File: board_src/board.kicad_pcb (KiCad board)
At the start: 2 copper layers, 113 parts, among them IC1 PCF8563TS_4,118, IC2 M24C02-WMN6TP, IC3 DS18B20+, IC5 MCP3202-CI_MS, J1 Conn_01x05, J10 Conn_01x01_Pin, J11 Conn_01x03, J12 112J-TDAR-R01, J13 Conn_01x03, J14 Conn_01x07, J15 Conn_01x03, J16 Conn_01x05, J17 Conn_01x05, J18 Conn_02x20_Counter_Clockwise, J19 Conn_02x07_Odd_Even, J2 Conn_01x05, J20 Conn_02x20_Counter_Clockwise, J21 Conn_02x20_Counter_Clockwise, J22 Conn_02x20_Counter_Clockwise, J23 Conn_01x04, J24 Conn_01x08, J25 Conn_01x04, J27 USB4135-GF-A, J29 Conn_01x08, J3 Conn_01x06, J30 Conn_01x05, J31 Conn_01x05, J4 Conn_01x04, J5 Conn_01x08, J6 Conn_01x03, J8 Conn_01x03, J9 Conn_01x02_Pin, Q1 NPN, Q2 SS8550, Q3 SS8550, Q4 SS8550, Q5 SS8550, Q6 BC107, U1 Pico, U4 Pico, Y2 Crystal

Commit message: wersja z FT232RN
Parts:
- removed BT1: 3012, footprints:3012
- removed C3, C7: 10uF, Capacitor_SMD:C_0201_0603Metric
- removed C5, C6: 100uF, Capacitor_SMD:C_0201_0603Metric
- removed D12, D13: 1N4148WT, Diode_SMD:D_SOD-523
- removed Q6: BC107, OptoDevice:Osram_SFH3710
- removed R17, R18: 4.7k, Resistor_SMD:R_0201_0603Metric
- added D1: D_Schottky, Diode_SMD:D_1206_3216Metric, F.Cu at (116.5, 18.3)
- added IC4: FT232RNL-TUBE, footprints:SOP65P780X200-28N, F.Cu at (29.9, 74.5)
- added J32: Conn_02x05_Odd_Even, Connector_PinHeader_2.54mm:PinHeader_2x05_P2.54mm_Vertical, F.Cu at (41.7, 71.8)
- added J7: Conn_01x16_Socket, Connector_PinSocket_2.54mm:PinSocket_1x16_P2.54mm_Vertical, F.Cu at (129.8, 124.3)
- added LED10: red, footprints:LEDC1608X80N, F.Cu at (37.3, 65.5)
- added LED11: green, footprints:LEDC1608X100N, F.Cu at (40.3, 65.6)
- added Q7: BC107, OptoDevice:Osram_SFH3710, F.Cu at (163.6, 162.2)
- added R4: R, Resistor_SMD:R_1206_3216Metric, F.Cu at (163.7, 164.2)
- added R43: 4.7k, Resistor_SMD:R_1206_3216Metric, F.Cu at (49.4, 32.9)
- added R44: 4.7k, Resistor_SMD:R_1206_3216Metric, F.Cu at (49.4, 35.2)
- added R5: 1k, Resistor_SMD:R_1206_3216Metric, F.Cu at (45.0, 64.2)
- added SW1: SW_MEC_5E, Button_Switch_THT:SW_PUSH_6mm_H9.5mm, F.Cu at (93.9, 158.7)
- C1: footprint Capacitor_SMD:C_0201_0603Metric -> Capacitor_SMD:C_1206_3216Metric
- C2: value C -> C_Small; footprint Capacitor_SMD:C_0201_0603Metric -> Capacitor_SMD:C_1206_3216Metric
- C4: footprint Capacitor_SMD:C_1808_4520Metric -> Capacitor_SMD:C_1206_3216Metric_Pad1.33x1.80mm_HandSolder
- J10: value Conn_01x01_Pin -> Conn_01x02_Pin; footprint Connector_PinHeader_2.54mm:PinHeader_1x01_P2.54mm_Vertical -> Connector_PinHeader_2.54mm:PinHeader_1x02_P2.54mm_Vertical
- J6: value Conn_01x03 -> Conn_01x02_Pin; footprint Connector_PinHeader_2.54mm:PinHeader_1x03_P2.54mm_Vertical -> Connector_PinHeader_2.54mm:PinHeader_1x02_P2.54mm_Vertical
- J8: value Conn_01x03 -> Conn_01x01_Pin; footprint Connector_PinHeader_2.54mm:PinHeader_1x03_P2.54mm_Vertical -> Connector_PinHeader_2.54mm:PinHeader_1x01_P2.54mm_Vertical
- R1, R11, R12, R14, R15, R16, R2, R20, R21, R22, R23, R35, R36, R37, R38, R39, R40, R41, R42: footprint Resistor_SMD:R_0201_0603Metric -> Resistor_SMD:R_1206_3216Metric
- R19: value 103 -> 10k; footprint Resistor_SMD:R_0201_0603Metric -> Resistor_SMD:R_1206_3216Metric
- R3: value R -> 1k; footprint Resistor_SMD:R_0201_0603Metric -> Resistor_SMD:R_1206_3216Metric
- R31, R32, R33, R34: value 103 -> 10k
- moved R3 221.9 mm to (45.0, 66.9), turned to 180 degrees
- moved PS1 166.7 mm to (21.1, 63.2)
- moved J8 146.4 mm to (16.3, 29.8), turned to 0 degrees
- moved S3 114.4 mm to (114.4, 78.9), turned to 90 degrees
- moved RV1 111.4 mm to (157.5, 164.5)
- moved S4 100.9 mm to (106.4, 78.9), turned to 90 degrees
- moved S1 97.1 mm to (46.6, 19.6), turned to 0 degrees
- moved DS4 93.3 mm to (129.8, 124.3)
- moved S2 91.8 mm to (61.5, 19.6), turned to 0 degrees
- moved J6 90.2 mm to (24.8, 36.6), turned to 180 degrees
- moved R2 88.8 mm to (21.3, 85.3), turned to 0 degrees
- moved S5 88.2 mm to (98.3, 78.9), turned to 90 degrees
- moved R14 88.0 mm to (21.3, 87.6), turned to 0 degrees
- moved J13 86.8 mm to (22.7, 99.1), turned to 180 degrees
- moved Q1 83.6 mm to (21.8, 107.8)
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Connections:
- net /b1 renamed VBUS
- net /b2 renamed VSYS
- net Net-(IC1-CLKOUT) renamed /Zegar czasu rzeczywistego RTC/CLKOUT
- net Net-(IC1-~{INT}) renamed /Zegar czasu rzeczywistego RTC/INT
- C2 pad 1: GND -> Net-(IC4-3V3OUT)
- C2 pad 2: Net-(D12-K) -> GND
- C4 pad 2: Net-(J4-Pin_1) -> GND
- DS4 pad 1: GND -> unconnected-(DS4-VSS-Pad1)
- DS4 pad 10: /Wyświetlacz LCD/D3 -> unconnected-(DS4-DB3-Pad10)
- DS4 pad 11: /Wyświetlacz LCD/D4 -> unconnected-(DS4-DB4-Pad11)
- DS4 pad 12: /Wyświetlacz LCD/D5 -> unconnected-(DS4-DB5-Pad12)
- DS4 pad 13: /Wyświetlacz LCD/D6 -> unconnected-(DS4-DB6-Pad13)
- DS4 pad 14: /Wyświetlacz LCD/D7 -> unconnected-(DS4-DB7-Pad14)
- DS4 pad 15: Net-(DS4-A_1) -> unconnected-(DS4-A_1-Pad15)
- DS4 pad 16: +3.3V -> unconnected-(DS4-K_1-Pad16)
- DS4 pad 2: +3.3V -> unconnected-(DS4-VDD-Pad2)
- DS4 pad 3: Net-(DS4-VO) -> unconnected-(DS4-VO-Pad3)
- DS4 pad 4: /Wyświetlacz LCD/RS -> unconnected-(DS4-RS-Pad4)
- DS4 pad 5: /Wyświetlacz LCD/R/W -> unconnected-(DS4-R/~{W}-Pad5)
- DS4 pad 6: /Wyświetlacz LCD/E -> unconnected-(DS4-E-Pad6)
- DS4 pad 7: /Wyświetlacz LCD/D0 -> unconnected-(DS4-DB0-Pad7)
- DS4 pad 8: /Wyświetlacz LCD/D1 -> unconnected-(DS4-DB1-Pad8)
- DS4 pad 9: /Wyświetlacz LCD/D2 -> unconnected-(DS4-DB2-Pad9)
- IC2 pad 7: Net-(IC2-~{WC}) -> GND
- J10 pad 1: Net-(IC2-~{WC}) -> Net-(IC1-SDA)
- J12 pad 6: GND -> +3.3V
- J27 pad A9: +3.3V -> Net-(D1-A)
- J27 pad B9: +3.3V -> +5V
- J4 pad 1: Net-(J4-Pin_1) -> Net-(IC5-VDD/VREF)
- J6 pad 1: Net-(J6-Pin_1) -> Net-(IC2-SDA)
- J6 pad 2: Net-(J6-Pin_2) -> Net-(IC2-SCL)
- J8 pad 1: Net-(J8-Pin_1) -> GND
- PS1 pad 5: +3.3V -> GND
- R3 pad 1: Net-(Q6-B) -> +5V
- R3 pad 2: /Wyświetlacz LCD/BL -> Net-(LED11-A)
- RV1 pad 2: Net-(DS4-VO) -> Net-(J7-Pin_3)
- U1 pad 41: Net-(J8-Pin_3) -> unconnected-(U1-SWCLK-Pad41)_1
- U1 pad 42: Net-(J8-Pin_2) -> unconnected-(U1-GND-Pad42)_1
- U1 pad 43: Net-(J8-Pin_1) -> unconnected-(U1-SWDIO-Pad43)_1
- U4 pad 41: Net-(J6-Pin_3) -> unconnected-(U4-SWCLK-Pad41)_1
- U4 pad 42: Net-(J6-Pin_2) -> unconnected-(U4-GND-Pad42)
- U4 pad 43: Net-(J6-Pin_1) -> unconnected-(U4-SWDIO-Pad43)_1
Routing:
- net Net-(J13-Pin_3): track 0.00 -> 13.5 mm
- net Net-(J13-Pin_2): track 0.00 -> 13.1 mm
- net Net-(VR2-WIPER): track 0.00 -> 13.0 mm
- net Net-(VR1-WIPER): track 0.00 -> 7.04 mm
- net Net-(J13-Pin_1): track 0.00 -> 6.30 mm
- net Net-(J8-Pin_3): track 5.31 -> 0.00 mm
- net Net-(J8-Pin_2): track 5.31 -> 0.00 mm
- net Net-(J8-Pin_1): track 5.31 -> 0.00 mm
- net Net-(J6-Pin_3): track 5.08 -> 0.00 mm
- net Net-(J6-Pin_2): track 5.08 -> 0.00 mm
- net Net-(J6-Pin_1): track 5.08 -> 0.00 mm
- net Net-(LS1-+): track 0.00 -> 4.89 mm
- net Net-(LED4-A): track 5.49 -> 1.23 mm
- net Net-(LED7-A): track 4.85 -> 0.89 mm
- net Net-(LED9-A): track 5.60 -> 1.65 mm
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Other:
- board text added: "BL"
- board text added: "BUZ"
- board text added: "C0"
- board text added: "C1"
- board text added: "CS"
- board text added: "D0"
- board text added: "D1"
- board text added: "D2"
- board text added: "D3"
- board text added: "D4"
- board text added: "D5"
- board text added: "D6"
- board text added: "D7"
- board text added: "DCD"
- board text added: "DSR"
- board text added: "DTR"
- board text added: "E"
- board text added: "E0"
- board text added: "MCP3202"
- board text added: "POT1"
- board text added: "POT2"
- board text added: "RI"
- board text added: "RS"
- board text added: "RTS"
- board text added: "RW"
- board text added: "RXD"
- board text added: "SCL"
- board text added: "SDA"
- board text added: "TXD"
- board text added: "VCC"
- board text removed: "WC"

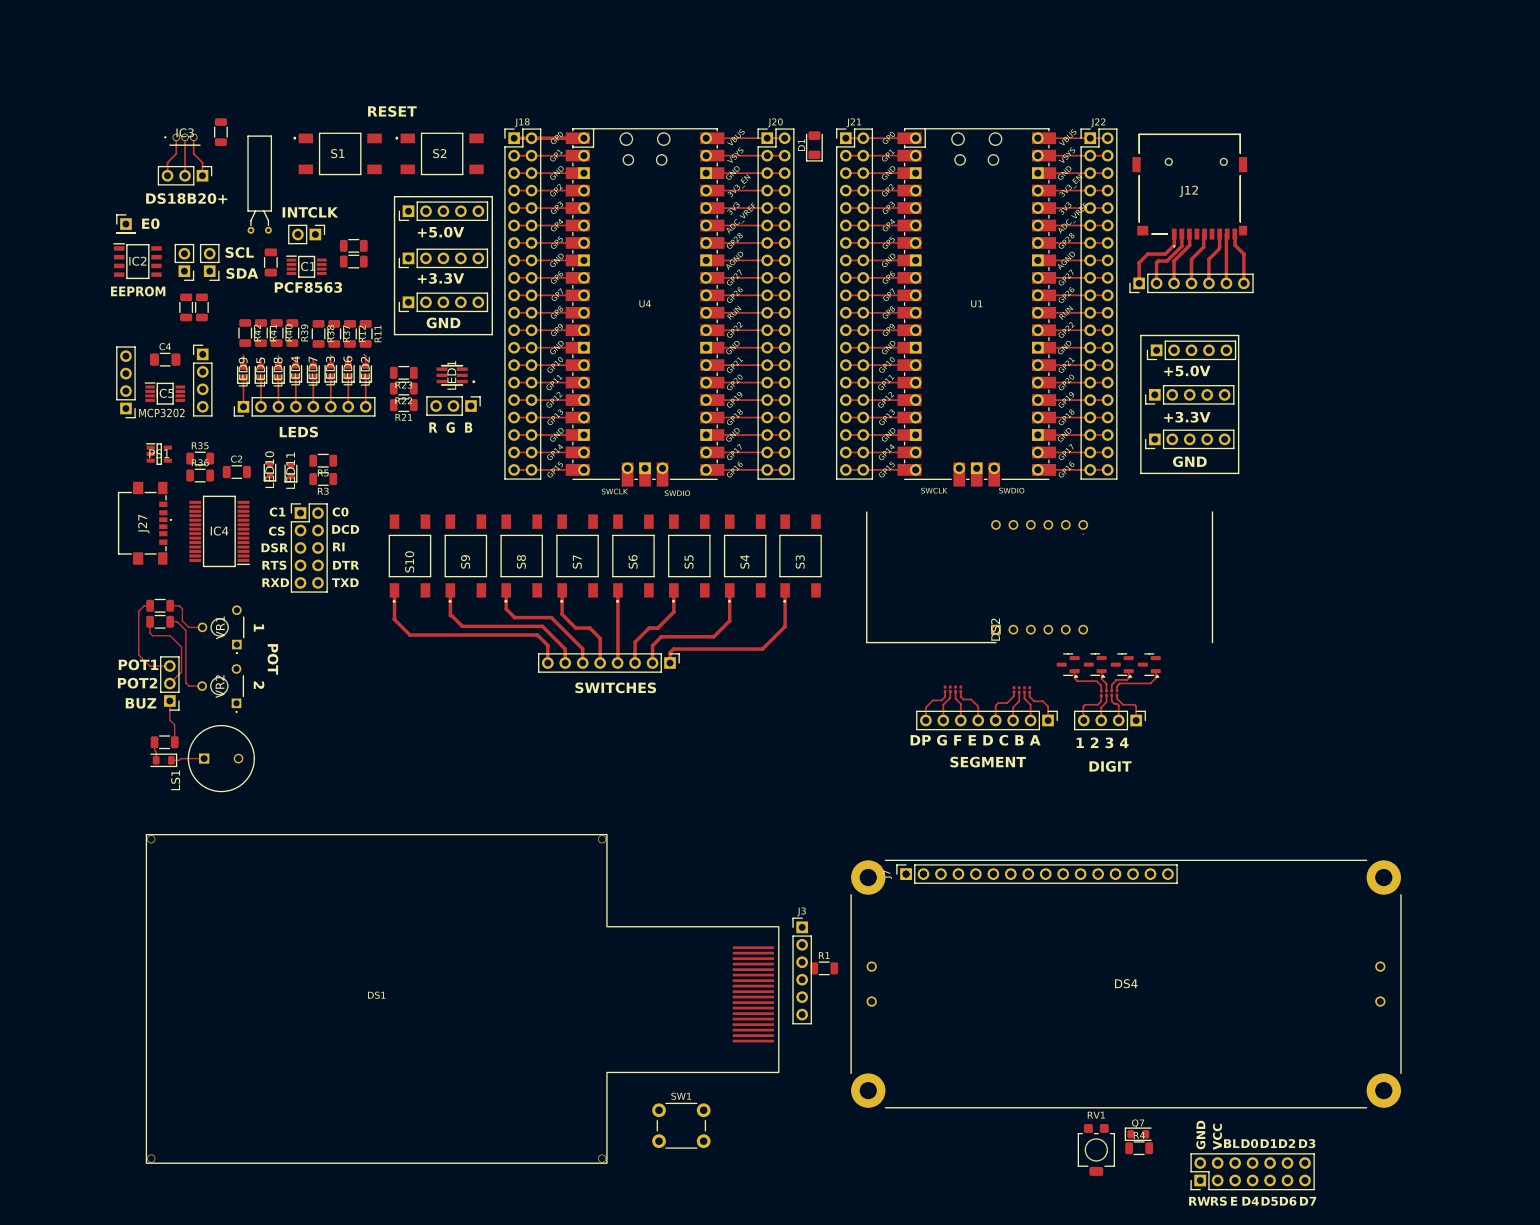
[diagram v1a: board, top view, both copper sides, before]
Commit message: Wersja ze sciezkami miedzianymi
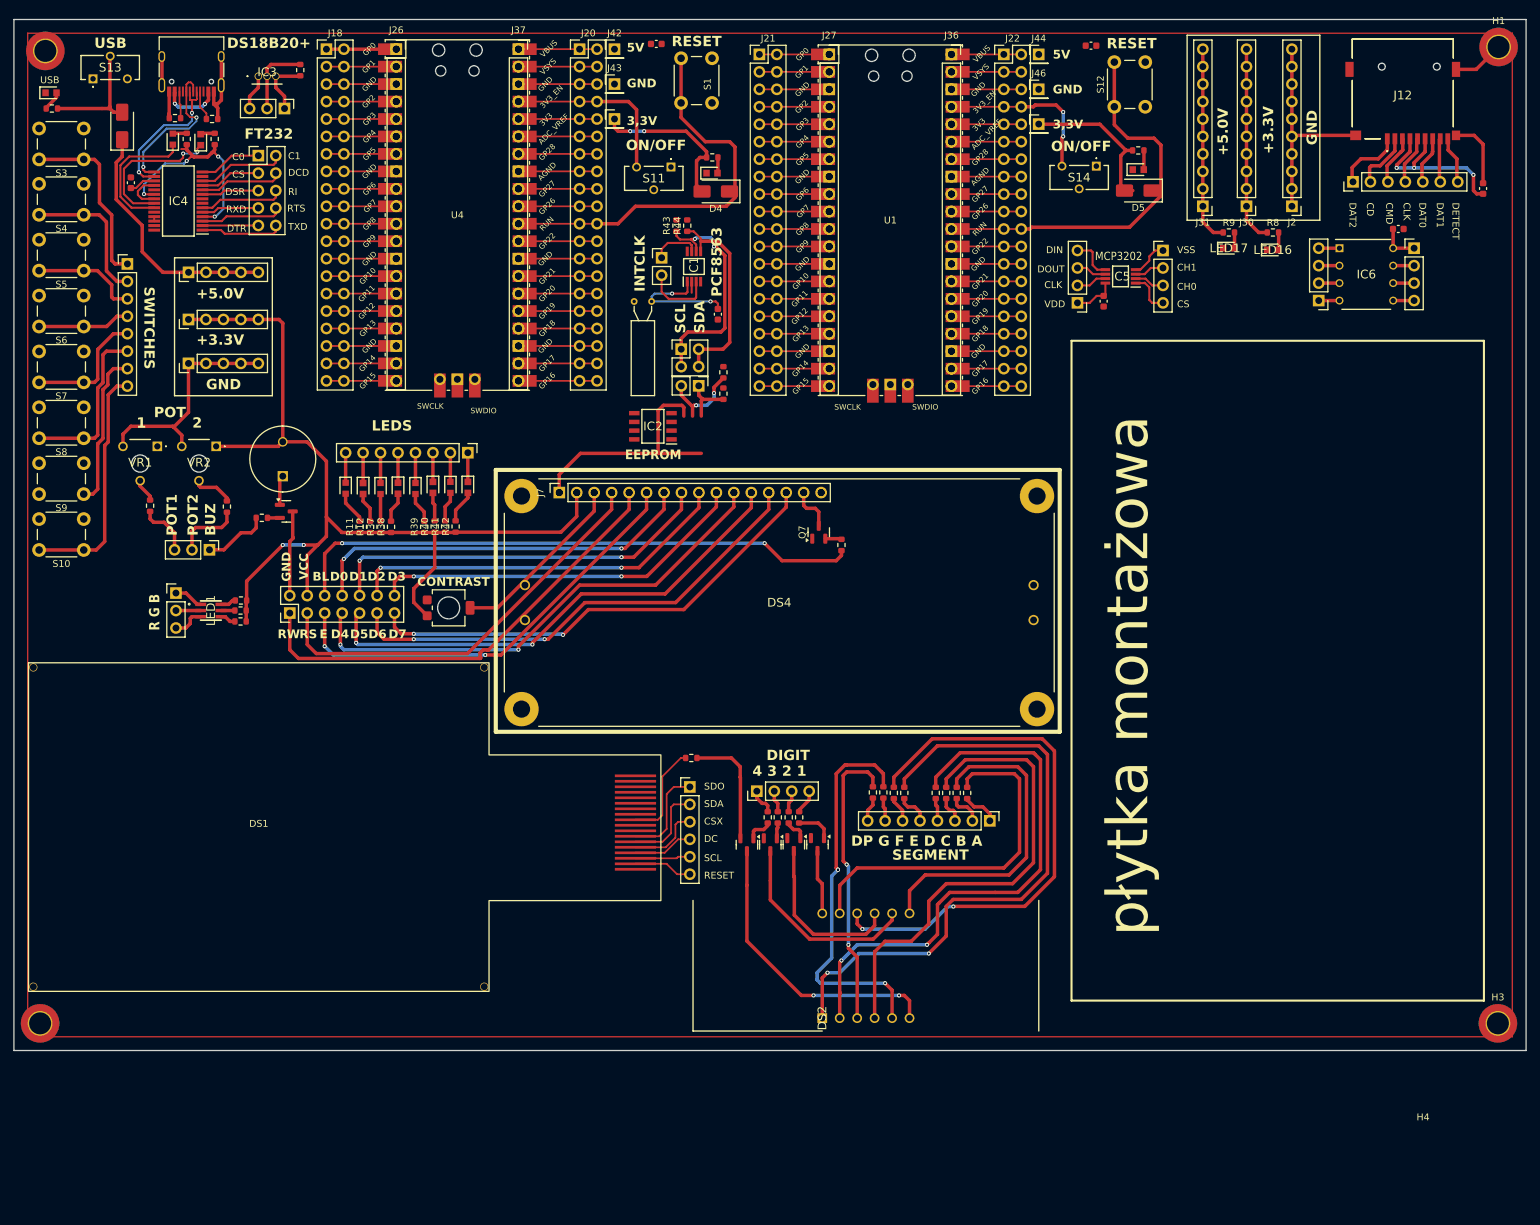
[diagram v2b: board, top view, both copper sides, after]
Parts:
- removed D1: D_Schottky, Diode_SMD:D_1206_3216Metric
- removed PS1: AP2202K-3.3TRG1, footprints:SOT95P282X145-5N
- removed R35, R36: 5.1k, Resistor_SMD:R_1206_3216Metric
- removed S2: 1301.9319, footprints:przycisk
- removed SW1: SW_MEC_5E, Button_Switch_THT:SW_PUSH_6mm_H9.5mm
- added C3: 100n, Capacitor_SMD:C_0603_1608Metric, F.Cu at (213.7, 24.6)
- added C5: 100n, Capacitor_SMD:C_0603_1608Metric, F.Cu at (93.5, 3.56)
- added C6: 100n, Capacitor_SMD:C_0603_1608Metric, F.Cu at (156.7, 3.81)
- added C7: 100n, Capacitor_SMD:C_0603_1608Metric, F.Cu at (201.4, 30.5)
- added D2: D_Schottky, Diode_SMD:D_SMA, F.Cu at (15.7, 15.5)
- added D4: D_Schottky, Diode_SMD:D_SMA, F.Cu at (102.1, 25.0)
- added D5: D_Schottky, Diode_SMD:D_SMA, F.Cu at (163.6, 24.9)
- added H1: MountingHole_Pad, MountingHole:MountingHole_3.2mm_M3_DIN965_Pad_TopBottom, F.Cu at (216.0, 4.00)
- added H2: MountingHole_Pad, MountingHole:MountingHole_3.2mm_M3_DIN965_Pad_TopBottom, F.Cu at (4.57, 4.57)
- added H3: MountingHole_Pad, MountingHole:MountingHole_3.2mm_M3_DIN965_Pad_TopBottom, F.Cu at (215.9, 146.1)
- added H4: MountingHole_Pad, MountingHole:MountingHole_3.2mm_M3_DIN965_Pad_TopBottom, F.Cu at (3.81, 146.1)
- added IC6: MCP4921-E_P, footprints:DIP781W56P254L950H533Q8N, F.Cu at (196.8, 37.1)
- added J26: Conn_01x20_Socket, Connector_PinSocket_2.54mm:PinSocket_1x20_P2.54mm_Vertical, F.Cu at (55.6, 4.32)
- added J28: Conn_01x04, Connector_PinHeader_2.54mm:PinHeader_1x04_P2.54mm_Vertical, F.Cu at (189.8, 40.9)
- added J34: USB_C_Receptacle_USB2.0_16P, Connector_USB:USB_C_Receptacle_HRO_TYPE-C-31-M-12, F.Cu at (25.8, 6.44)
- added J36: Conn_01x20_Socket, Connector_PinSocket_2.54mm:PinSocket_1x20_P2.54mm_Vertical, F.Cu at (136.4, 5.08)
- added J37: Conn_01x20_Socket, Connector_PinSocket_2.54mm:PinSocket_1x20_P2.54mm_Vertical, F.Cu at (73.4, 4.32)
- added J40: Conn_01x01_Pin, Connector_PinHeader_2.54mm:PinHeader_1x01_P2.54mm_Vertical, F.Cu at (87.4, 14.5)
- added J41: Conn_01x01_Pin, Connector_PinHeader_2.54mm:PinHeader_1x01_P2.54mm_Vertical, F.Cu at (149.1, 15.2)
- added J42: Conn_01x01_Pin, Connector_PinHeader_2.54mm:PinHeader_1x01_P2.54mm_Vertical, F.Cu at (87.4, 4.32)
- added J43: Conn_01x01_Pin, Connector_PinHeader_2.54mm:PinHeader_1x01_P2.54mm_Vertical, F.Cu at (87.4, 9.40)
- added J44: Conn_01x01_Pin, Connector_PinHeader_2.54mm:PinHeader_1x01_P2.54mm_Vertical, F.Cu at (149.1, 5.08)
- added J46: Conn_01x01_Pin, Connector_PinHeader_2.54mm:PinHeader_1x01_P2.54mm_Vertical, F.Cu at (149.1, 10.2)
- added LED14: green, footprints:LEDC1608X100N, F.Cu at (101.6, 22.4)
- added LED15: green, footprints:LEDC1608X100N, F.Cu at (163.6, 21.8)
- added LED16: green, footprints:LEDC1608X100N, F.Cu at (183.1, 33.5)
- added LED17: green, footprints:LEDC1608X100N, F.Cu at (176.7, 33.3)
- added LED18: green, footprints:LEDC1608X100N, F.Cu at (5.40, 10.7)
- added R10: 249, Resistor_SMD:R_0603_1608Metric, F.Cu at (5.53, 13.0)
- added R45: 5.1k, Resistor_SMD:R_0603_1608Metric, F.Cu at (28.8, 14.5)
- added R46: 5.1k, Resistor_SMD:R_0603_1608Metric, F.Cu at (23.4, 14.4)
- added R6: 249, Resistor_SMD:R_0603_1608Metric, F.Cu at (101.6, 20.1)
- added R7: 249, Resistor_SMD:R_0603_1608Metric, F.Cu at (163.6, 19.1)
- added R8: 249, Resistor_SMD:R_0603_1608Metric, F.Cu at (183.2, 31.0)
- added R9: 249, Resistor_SMD:R_0603_1608Metric, F.Cu at (176.8, 31.0)
- added S11: CL-SB-12C-01, footprints:CLSB12C01, F.Cu at (95.6, 21.5)
- added S12: 1301.9319, Button_Switch_THT:SW_PUSH_6mm_H9.5mm, F.Cu at (160.1, 12.7)
- added S13: CL-SB-12C-01, footprints:CLSB12C01, F.Cu at (11.5, 8.64)
- added S14: CL-SB-12C-01, footprints:CLSB12C01, F.Cu at (157.5, 21.3)
- C1: value C -> 100n; footprint Capacitor_SMD:C_1206_3216Metric -> Capacitor_SMD:C_0603_1608Metric
- C2: footprint Capacitor_SMD:C_1206_3216Metric -> Capacitor_SMD:C_0603_1608Metric
- C4: footprint Capacitor_SMD:C_1206_3216Metric_Pad1.33x1.80mm_HandSolder -> Capacitor_SMD:C_0603_1608Metric
- J10: footprint Connector_PinHeader_2.54mm:PinHeader_1x02_P2.54mm_Vertical -> Connector_PinHeader_2.54mm:PinHeader_2x02_P2.54mm_Vertical
- J2, J30, J31: footprint Connector_PinHeader_2.54mm:PinHeader_1x05_P2.54mm_Vertical -> Connector_PinHeader_2.54mm:PinHeader_1x10_P2.54mm_Vertical
- J27: value USB4135-GF-A -> Conn_01x20_Socket; footprint footprints:USB4135GFA -> Connector_PinSocket_2.54mm:PinSocket_1x20_P2.54mm_Vertical
- J8: value Conn_01x01_Pin -> Conn_01x04; footprint Connector_PinHeader_2.54mm:PinHeader_1x01_P2.54mm_Vertical -> Connector_PinHeader_2.54mm:PinHeader_1x04_P2.54mm_Vertical
- Q1, Q7: footprint OptoDevice:Osram_SFH3710 -> Package_TO_SOT_SMD:SOT-23
- R1, R14, R15, R16, R19, R2, R20, R21, R22, R23, R3, R4, R43, R44, R5: footprint Resistor_SMD:R_1206_3216Metric -> Resistor_SMD:R_0603_1608Metric
- R11, R12, R37, R38, R39, R40, R41, R42: value 68 -> 221; footprint Resistor_SMD:R_1206_3216Metric -> Resistor_SMD:R_0603_1608Metric
- R13, R24, R25, R26, R27, R28, R29, R30, R31, R32, R33, R34: footprint Resistor_SMD:R_0201_0603Metric -> Resistor_SMD:R_0603_1608Metric
- S1, S10, S3, S4, S5, S6, S7, S8, S9: footprint footprints:przycisk -> Button_Switch_THT:SW_PUSH_6mm_H9.5mm
- moved J8 187.4 mm to (203.7, 33.3)
- moved J19 156.1 mm to (40.1, 86.4)
- moved J23 152.6 mm to (167.2, 33.6), turned to 0 degrees
- moved IC5 140.0 mm to (161.0, 37.4), turned to 180 degrees
- moved C4 136.8 mm to (158.5, 41.0), turned to -90 degrees
- moved J4 127.5 mm to (154.7, 41.2), turned to 180 degrees
- moved RV1 122.9 mm to (63.2, 85.6), turned to 90 degrees
- moved J27 121.0 mm to (118.6, 5.08), turned to 0 degrees
- moved S3 119.6 mm to (10.2, 20.4), turned to 180 degrees
- moved S4 108.7 mm to (10.2, 28.4), turned to 180 degrees
- moved Q7 99.2 mm to (117.1, 74.6), turned to 90 degrees
- moved J5 98.0 mm to (16.5, 35.6), turned to 0 degrees
- moved R4 97.9 mm to (120.4, 76.5), turned to -90 degrees
- moved S5 97.8 mm to (10.2, 36.5), turned to 180 degrees
- moved S6 87.0 mm to (10.2, 44.7), turned to 180 degrees
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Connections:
- IC4 pad 15: unconnected-(IC4-USBDP-Pad15) -> Net-(IC4-USBDP)
- IC4 pad 16: unconnected-(IC4-USBDM-Pad16) -> Net-(IC4-USBDM)
- J10 pad 1: Net-(IC1-SDA) -> Net-(IC1-SCL)
- J10 pad 2: Net-(IC1-SCL) -> Net-(IC1-SDA)
- J17 pad 1: +5.0V -> VSYS
- J17 pad 2: +5.0V -> VSYS
- J17 pad 3: +5.0V -> VSYS
- J17 pad 4: +5.0V -> VSYS
- J17 pad 5: +5.0V -> VSYS
- J20 pad 1: VBUS -> /b1
- J20 pad 2: VBUS -> /b1
- J22 pad 3: /d2 -> VSYS
- J22 pad 4: /d2 -> VSYS
- J30 pad 1: +3.3V -> Net-(J30-Pin_1)
- J30 pad 2: +3.3V -> Net-(J30-Pin_1)
- J30 pad 3: +3.3V -> Net-(J30-Pin_1)
- J30 pad 4: +3.3V -> Net-(J30-Pin_1)
- J30 pad 5: +3.3V -> Net-(J30-Pin_1)
- J31 pad 1: +5.0V -> Net-(J31-Pin_1)
- J31 pad 2: +5.0V -> Net-(J31-Pin_1)
- J31 pad 3: +5.0V -> Net-(J31-Pin_1)
- J31 pad 4: +5.0V -> Net-(J31-Pin_1)
- J31 pad 5: +5.0V -> Net-(J31-Pin_1)
- J32 pad 1: /Port USB/C4 -> /Port USB/C3
- J32 pad 2: /Port USB/C3 -> /Port USB/C4
- J32 pad 7: /Port USB/RTS -> /Port USB/RXD
- J32 pad 8: /Port USB/DTR -> /Port USB/RTS
- J32 pad 9: /Port USB/RXD -> /Port USB/DTR
- J8 pad 1: GND -> Net-(IC6-VOUT)
- R14 pad 2: Net-(VR2-WIPER) -> Net-(R14-Pad2)
- R2 pad 2: Net-(VR1-WIPER) -> Net-(R2-Pad2)
- S1 pad 1: GND -> /b11
- U1 pad 1: /c1 -> unconnected-(U1-GPIO0-Pad1)_1
- U1 pad 10: /c10 -> unconnected-(U1-GPIO7-Pad10)_1
- U1 pad 11: /c11 -> unconnected-(U1-GPIO8-Pad11)_1
- U1 pad 12: /c12 -> unconnected-(U1-GPIO9-Pad12)
- U1 pad 13: /c13 -> unconnected-(U1-GND-Pad13)_1
- U1 pad 14: /c14 -> unconnected-(U1-GPIO10-Pad14)
- U1 pad 15: /c15 -> unconnected-(U1-GPIO11-Pad15)_1
- U1 pad 16: /c16 -> unconnected-(U1-GPIO12-Pad16)
- U1 pad 17: /c17 -> unconnected-(U1-GPIO13-Pad17)_1
- U1 pad 18: /c18 -> unconnected-(U1-GND-Pad18)_1
- U1 pad 19: /c19 -> unconnected-(U1-GPIO14-Pad19)
- U1 pad 2: /c2 -> unconnected-(U1-GPIO1-Pad2)
- U1 pad 20: /c20 -> unconnected-(U1-GPIO15-Pad20)
- U1 pad 21: /d20 -> unconnected-(U1-GPIO16-Pad21)
- U1 pad 22: /d19 -> unconnected-(U1-GPIO17-Pad22)
- U1 pad 23: /d18 -> unconnected-(U1-GND-Pad23)
- U1 pad 24: /d17 -> unconnected-(U1-GPIO18-Pad24)
- U1 pad 25: /d16 -> unconnected-(U1-GPIO19-Pad25)
- U1 pad 26: /d15 -> unconnected-(U1-GPIO20-Pad26)_1
- U1 pad 27: /d14 -> unconnected-(U1-GPIO21-Pad27)
- U1 pad 28: /d13 -> unconnected-(U1-GND-Pad28)_1
- U1 pad 29: /d12 -> unconnected-(U1-GPIO22-Pad29)
- U1 pad 3: /c3 -> unconnected-(U1-GND-Pad3)
- U1 pad 30: /d11 -> unconnected-(U1-RUN-Pad30)
- U1 pad 31: /d10 -> unconnected-(U1-GPIO26_ADC0-Pad31)_1
- U1 pad 32: /d9 -> unconnected-(U1-GPIO27_ADC1-Pad32)_1
- U1 pad 33: /d8 -> unconnected-(U1-AGND-Pad33)
- U1 pad 34: /d7 -> unconnected-(U1-GPIO28_ADC2-Pad34)
- U1 pad 35: /d6 -> unconnected-(U1-ADC_VREF-Pad35)_1
- U1 pad 36: /d5 -> unconnected-(U1-3V3-Pad36)_1
- U1 pad 37: /d4 -> unconnected-(U1-3V3_EN-Pad37)_1
- U1 pad 38: /d3 -> unconnected-(U1-GND-Pad38)_1
- U1 pad 39: /d2 -> unconnected-(U1-VSYS-Pad39)
- U1 pad 4: /c4 -> unconnected-(U1-GPIO2-Pad4)_1
- U1 pad 40: /d1 -> unconnected-(U1-VBUS-Pad40)_1
- U1 pad 5: /c5 -> unconnected-(U1-GPIO3-Pad5)_1
- U1 pad 6: /c6 -> unconnected-(U1-GPIO4-Pad6)_1
- U1 pad 7: /c7 -> unconnected-(U1-GPIO5-Pad7)_1
- U1 pad 8: /c8 -> unconnected-(U1-GND-Pad8)_1
- U1 pad 9: /c9 -> unconnected-(U1-GPIO6-Pad9)
- U4 pad 1: /a1 -> unconnected-(U4-GPIO0-Pad1)
- U4 pad 10: /a10 -> unconnected-(U4-GPIO7-Pad10)_1
- U4 pad 11: /a11 -> unconnected-(U4-GPIO8-Pad11)
- U4 pad 12: /a12 -> unconnected-(U4-GPIO9-Pad12)
- U4 pad 13: /a13 -> unconnected-(U4-GND-Pad13)_1
- U4 pad 14: /a14 -> unconnected-(U4-GPIO10-Pad14)_1
- U4 pad 15: /a15 -> unconnected-(U4-GPIO11-Pad15)
- U4 pad 16: /a16 -> unconnected-(U4-GPIO12-Pad16)_1
- U4 pad 17: /a17 -> unconnected-(U4-GPIO13-Pad17)_1
- U4 pad 18: /a18 -> unconnected-(U4-GND-Pad18)_1
- U4 pad 19: /a19 -> unconnected-(U4-GPIO14-Pad19)_1
- U4 pad 2: /a2 -> unconnected-(U4-GPIO1-Pad2)
- U4 pad 20: /a20 -> unconnected-(U4-GPIO15-Pad20)
- U4 pad 21: /b20 -> unconnected-(U4-GPIO16-Pad21)
- U4 pad 22: /b19 -> unconnected-(U4-GPIO17-Pad22)
- U4 pad 23: /b18 -> unconnected-(U4-GND-Pad23)_1
- U4 pad 24: /b17 -> unconnected-(U4-GPIO18-Pad24)_1
- U4 pad 25: /b16 -> unconnected-(U4-GPIO19-Pad25)_1
- U4 pad 26: /b15 -> unconnected-(U4-GPIO20-Pad26)_1
- U4 pad 27: /b14 -> unconnected-(U4-GPIO21-Pad27)_1
- U4 pad 28: /b13 -> unconnected-(U4-GND-Pad28)
- U4 pad 29: /b12 -> unconnected-(U4-GPIO22-Pad29)
- U4 pad 3: /a3 -> unconnected-(U4-GND-Pad3)
- U4 pad 30: /b11 -> unconnected-(U4-RUN-Pad30)
- U4 pad 31: /b10 -> unconnected-(U4-GPIO26_ADC0-Pad31)
- U4 pad 32: /b9 -> unconnected-(U4-GPIO27_ADC1-Pad32)
- U4 pad 33: /b8 -> unconnected-(U4-AGND-Pad33)_1
- U4 pad 34: /b7 -> unconnected-(U4-GPIO28_ADC2-Pad34)_1
- U4 pad 35: /b6 -> unconnected-(U4-ADC_VREF-Pad35)
- U4 pad 36: /b5 -> unconnected-(U4-3V3-Pad36)
- U4 pad 37: /b4 -> unconnected-(U4-3V3_EN-Pad37)
- U4 pad 38: /b3 -> unconnected-(U4-GND-Pad38)_1
- U4 pad 39: VSYS -> unconnected-(U4-VSYS-Pad39)
- U4 pad 4: /a4 -> unconnected-(U4-GPIO2-Pad4)
- U4 pad 40: VBUS -> unconnected-(U4-VBUS-Pad40)
- U4 pad 5: /a5 -> unconnected-(U4-GPIO3-Pad5)_1
- U4 pad 6: /a6 -> unconnected-(U4-GPIO4-Pad6)
- U4 pad 7: /a7 -> unconnected-(U4-GPIO5-Pad7)
- U4 pad 8: /a8 -> unconnected-(U4-GND-Pad8)
- U4 pad 9: /a9 -> unconnected-(U4-GPIO6-Pad9)_1
- VR1 pad A1: +3.3V -> (no net)
- VR1 pad E1: GND -> (no net)
- VR1 pad S1: Net-(VR1-WIPER) -> (no net)
- VR2 pad A1: +3.3V -> (no net)
- VR2 pad E1: GND -> (no net)
- VR2 pad S1: Net-(VR2-WIPER) -> (no net)
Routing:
- net +3.3V: track 6.11 -> 195.5 mm, vias 0 -> 5
- net GND: track 6.11 -> 165.6 mm
- net /Wyświetlacz segmentowy/e: track 0.00 -> 89.3 mm, vias 0 -> 2
- net /Wyświetlacz LCD/BL: track 0.00 -> 84.0 mm, vias 0 -> 2
- net /Wyświetlacz segmentowy/d: track 0.00 -> 80.7 mm, vias 0 -> 2
- net /Wyświetlacz segmentowy/f: track 0.00 -> 80.3 mm, vias 0 -> 2
- net /Wyświetlacz LCD/D4: track 0.00 -> 73.4 mm, vias 0 -> 2
- net /Wyświetlacz LCD/D5: track 0.00 -> 72.7 mm, vias 0 -> 2
- net /Wyświetlacz LCD/D6: track 0.00 -> 70.5 mm, vias 0 -> 2
- net /Wyświetlacz segmentowy/c: track 0.00 -> 69.5 mm
- net /Wyświetlacz LCD/D7: track 0.00 -> 69.3 mm, vias 0 -> 2
- net /Wyświetlacz LCD/R/W: track 0.00 -> 67.3 mm
- net /Wyświetlacz LCD/E: track 0.00 -> 63.4 mm, vias 0 -> 2
- net /Wyświetlacz LCD/RS: track 0.00 -> 60.5 mm
- net /Wyświetlacz LCD/D1: track 0.00 -> 57.5 mm, vias 0 -> 2
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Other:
- board outline added: 220 x 150 mm
- board text added: "3,3V"
- board text added: "4 3 2 1"
- board text added: "5V"
- board text added: "CD"
- board text added: "CH0"
- board text added: "CH1"
- board text added: "CMD"
- board text added: "CONTRAST"
- board text added: "CSX"
- board text added: "DAT0"
- board text added: "DAT1"
- board text added: "DAT2"
- board text added: "DC"
- board text added: "DETECT"
- board text added: "DIN"
- board text added: "DOUT"
- board text added: "FT232"
- board text added: "ON/OFF"
- board text added: "SDO"
- board text added: "USB"
- board text added: "VDD"
- board text added: "VSS"
- board text added: "płytka montażowa"
- board text removed: "1 2 3 4"
- board text removed: "E0"

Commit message: sciezki polaczen
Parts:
- moved U4 212.3 mm to (276.1, 11.2)
- moved DS4 160.4 mm to (238.3, 47.2)
- moved U1 116.7 mm to (242.8, 11.4)
- moved J37 48.3 mm to (72.6, 52.6), turned to 180 degrees
- moved J36 47.0 mm to (138.7, 52.1), turned to 180 degrees
- moved IC2 27.2 mm to (101.9, 33.5)
- moved R16 23.9 mm to (95.6, 31.8), turned to 180 degrees
- moved J9 22.3 mm to (95.5, 56.9), turned to 180 degrees
- moved R44 19.7 mm to (104.6, 48.5), turned to 0 degrees
- moved R15 19.6 mm to (95.6, 33.3), turned to 180 degrees
- moved IC1 19.0 mm to (102.0, 54.7), turned to 0 degrees
- moved R43 18.7 mm to (99.1, 48.5), turned to 180 degrees
- moved J6 13.1 mm to (103.1, 40.6)
- moved Y2 9.58 mm to (93.8, 49.9), turned to 180 degrees
- moved C1 9.05 mm to (96.0, 49.3), turned to -90 degrees
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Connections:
- Q1 pad 1: Net-(LS1-+) -> Net-(Q1-B)
- Q1 pad 2: Net-(Q1-B) -> GND
- Q1 pad 3: GND -> Net-(LS1-+)
- Y2 pad 1: Net-(IC1-OSCO) -> Net-(IC1-OSCI)
- Y2 pad 2: Net-(IC1-OSCI) -> Net-(IC1-OSCO)
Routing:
- net GND: track 165.6 -> 830.0 mm, vias 0 -> 13
- net +3.3V: track 195.5 -> 485.9 mm, vias 5 -> 17
- net +5V: track 31.8 -> 240.6 mm
- net VSYS: track 47.8 -> 210.6 mm, vias 0 -> 2
- net /Wyświetlacz segmentowy/f: track 80.3 -> 14.5 mm, vias 2 -> 1
- net /Wyświetlacz segmentowy/e: track 89.3 -> 46.6 mm, vias 2 -> 1
- net /Wyświetlacz segmentowy/d: track 80.7 -> 41.9 mm, vias 2 -> 1
- net /Wyświetlacz segmentowy/c: track 69.5 -> 36.8 mm, vias 0 -> 1
- net /Wyświetlacz segmentowy/b: track 46.9 -> 17.3 mm, vias 0 -> 1
- net /Wyświetlacz segmentowy/a: track 52.4 -> 28.5 mm, vias 0 -> 2
- net /Wyświetlacz segmentowy/g: track 56.8 -> 39.2 mm, vias 3 -> 1
- net /d11: track 57.0 -> 40.7 mm, vias 0 -> 1
- net Net-(IC1-SCL): track 33.3 -> 17.6 mm, vias 2 -> 0
- net /b11: track 58.7 -> 43.2 mm, vias 0 -> 1
- net Net-(IC1-SDA): track 29.7 -> 16.1 mm
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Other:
- board text added: "3.3V"
- board text added: "DP"
- board text added: "G F E D C B A"
- board text added: "LDAC"
- board text added: "MCP4921"
- board text added: "MICRO SD"
- board text added: "SCK"
- board text added: "SDI"
- board text added: "VOUT"
- board text added: "VREF"
- board text removed: "DP G F E D C B A"
